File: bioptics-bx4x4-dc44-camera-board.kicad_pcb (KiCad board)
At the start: 4 copper layers, 260 x 187 mm, 475 parts, among them J1 RadEye1, J10 RadEye1, J11 RadEye1, J12 TagConnect_TC2030_SWD, J13 RadEye1, J14 RadEye1, J2 RadEye1, J3 USB_C_Receptacle_USB2.0, J4 TagConnect_TC2030_SWD, J5 TagConnect_TC2030_SWD, J6 TagConnect_TC2030_SWD, J7 RadEye1, J8 RadEye1, J9 TagConnect_TC2030_SWD, U1 AMS1117-3.3, U10 SRV05-4, U11 IS4xS32160F-xTL, U12 USB3300-EZK, U13 AMS1117-3.3, U14 STM32H753IITx, U15 CJ431, U16 7408, U17 CJ431, U18 AMS1117-3.3, U19 STM32H753IITx, U2 STM32H753IITx, U20 7408, U21 SN74AVC8T245PW, U22 AD5112, U23 INA849, U24 SN74AVC8T245PW, U25 AD5112, U26 INA849, U28 AMS1117-3.3, U29 STM32H753IITx, U3 SN74AVC8T245PW, U30 7408, U31 SN74AVC8T245PW, U32 AD5112, U33 INA849, U34 SN74AVC8T245PW, U35 AD5112, U36 INA849, U38 AMS1117-3.3, U39 STM32H753IITx, U4 AD5112, U40 7408, U41 SN74AVC8T245PW, U42 AD5112, U43 INA849, U44 SN74AVC8T245PW, U45 AD5112, U46 INA849, U5 INA849, U6 SN74AVC8T245PW, U7 AD5112, U8 INA849, U9 FP6291, Y1 24MHz

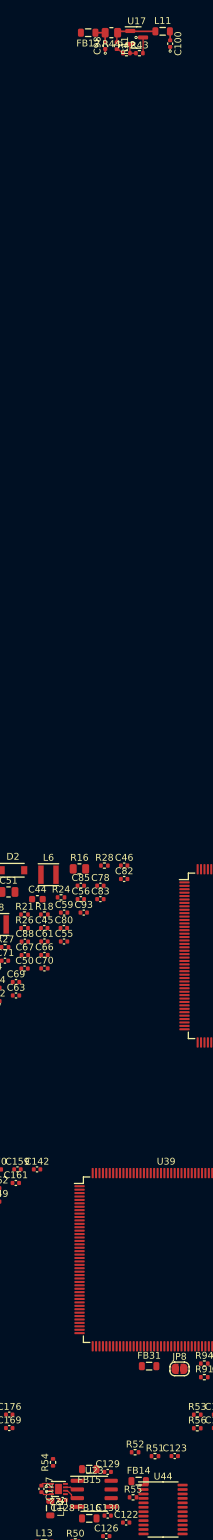
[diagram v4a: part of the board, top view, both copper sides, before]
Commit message: Delete PoC layouts on unplaced parts
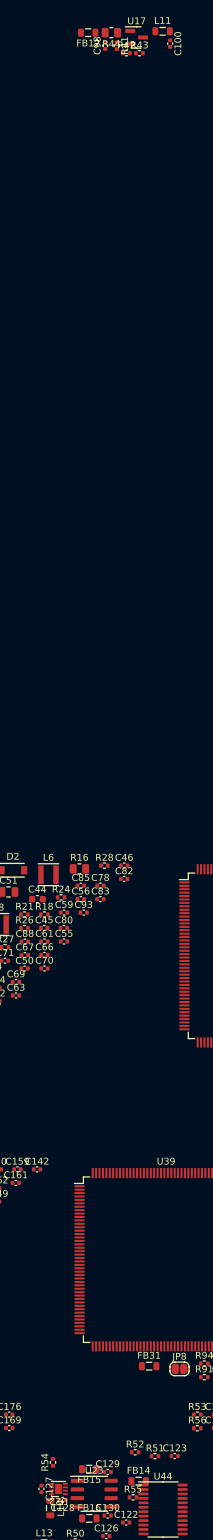
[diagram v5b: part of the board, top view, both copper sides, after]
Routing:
- net Net-(L11-Pad1): track 7.01 -> 0.00 mm
- net GND: track 209.4 -> 203.1 mm, vias 58 -> 55
- net Net-(U22-Pad2): track 3.59 -> 0.00 mm
- net Net-(C98-Pad2): track 2.89 -> 0.00 mm
- net Net-(R42-Pad2): track 2.19 -> 0.00 mm
- net /Sensor board 2/3v3: track 1.64 -> 0.00 mm
- net /3v8_2: track 1.32 -> 0.00 mm
- net Net-(R41-Pad2): track 0.94 -> 0.00 mm
- net /Sensor board 2/SCL_{1}: track 0.83 -> 0.00 mm, vias 1 -> 0
- net /Sensor board 2/SDA_{1}: track 0.78 -> 0.00 mm, vias 1 -> 0
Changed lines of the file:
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@@
   (segment (start 65.124168 32.58) (end 64.904168 32.8) (width 0.127) (layer "F.Cu") (net 4))
   (segment (start 120.4 65.288957) (end 120.4 65.258957) (width 0.127) (layer "F.Cu") (net 4))
-  (segment (start 440.0775 -55.44) (end 440.0775 -53.1775) (width 0.127) (layer "F.Cu") (net 4))
   (segment (start 48.6625 70.5) (end 48.6625 68.2375) (width 0.127) (layer "F.Cu") (net 4))
   (segment (start 120.4 65.258957) (end 121.55 64.108958) (width 0.127) (layer "F.Cu") (net 4))
@@
   (segment (start 34.983078 34.717499) (end 33.532501 34.717499) (width 0.127) (layer "F.Cu") (net 4))
   (segment (start 61.870062 52.935) (end 61.870062 55.785) (width 0.127) (layer "F.Cu") (net 4))
-  (segment (start 425.2 156.5) (end 425.2 156.4) (width 0.127) (layer "F.Cu") (net 4))
   (segment (start 106.2 36.058958) (end 106.199999 34.308957) (width 0.127) (layer "F.Cu") (net 4))
   (segment (start 53.3125 59.7) (end 53.3375 59.675) (width 0.127) (layer "F.Cu") (net 4))
@@
   (segment (start 49.475 47.100001) (end 50.5125 47.100001) (width 0.127) (layer "F.Cu") (net 4))
   (segment (start 114.28 35.288957) (end 114.25 35.258956) (width 0.127) (layer "F.Cu") (net 4))
-  (segment (start 425.2 156.4) (end 425.4 156.2) (width 0.127) (layer "F.Cu") (net 4))
   (segment (start 33.516922 56.233272) (end 34.996922 56.233272) (width 0.127) (layer "F.Cu") (net 4))
   (segment (start 98.67 56.858958) (end 98.1 56.858958) (width 0.127) (layer "F.Cu") (net 4))
@@
   (segment (start 35.67 49.935) (end 35.67 51.37) (width 0.127) (layer "F.Cu") (net 4))
   (segment (start 108.03 33.913957) (end 108 33.883957) (width 0.127) (layer "F.Cu") (net 4))
-  (segment (start 434.540001 -53.76) (end 434.54 -53.14) (width 0.254) (layer "F.Cu") (net 4))
   (segment (start 54.199999 68.82) (end 54.2 68.2) (width 0.254) (layer "F.Cu") (net 4))
   (segment (start 61.270062 50.62) (end 61.270062 49.335) (width 0.127) (layer "F.Cu") (net 4))
   (segment (start 137.075 48.93) (end 138.73 48.93) (width 0.127) (layer "F.Cu") (net 4))
-  (segment (start 440.0775 -53.1775) (end 440.04 -53.14) (width 0.127) (layer "F.Cu") (net 4))
   (segment (start 48.6625 68.2375) (end 48.7 68.2) (width 0.127) (layer "F.Cu") (net 4))
   (segment (start 126.475 44.408957) (end 127.949999 44.408957) (width 0.127) (layer "F.Cu") (net 4))
@@
   (segment (start 128 40.228957) (end 128.67 40.228956) (width 0.127) (layer "F.Cu") (net 4))
   (segment (start 120.4 65.288957) (end 120.4 65.958957) (width 0.127) (layer "F.Cu") (net 4))
-  (segment (start 425.4 156.2) (end 426.7 156.2) (width 0.127) (layer "F.Cu") (net 4))
   (segment (start 50.5125 47.100001) (end 50.5375 47.075001) (width 0.127) (layer "F.Cu") (net 4))
   (segment (start 35.67 51.37) (end 35.7 51.4) (width 0.127) (layer "F.Cu") (net 4))
@@
   (segment (start 137.075 47.66) (end 137.135 47.6) (width 0.127) (layer "F.Cu") (net 4))
   (segment (start 48.6625 70.5) (end 49.7 70.5) (width 0.254) (layer "F.Cu") (net 4))
-  (segment (start 440.0775 -55.44) (end 439.04 -55.44) (width 0.254) (layer "F.Cu") (net 4))
   (segment (start 55.2 47.750001) (end 54.1625 47.750001) (width 0.127) (layer "F.Cu") (net 4))
   (segment (start 67.837499 36.45) (end 67.0375 36.45) (width 0.127) (layer "F.Cu") (net 4))
@@
   (segment (start 132.125 54.01) (end 132.125 54.775) (width 0.127) (layer "F.Cu") (net 4))
   (segment (start 61.270062 50.835) (end 61.270062 50.585) (width 0.127) (layer "F.Cu") (net 4))
-  (segment (start 444.04 -54.06) (end 444.04 -53.44) (width 0.254) (layer "F.Cu") (net 4))
   (segment (start 44.7 69.12) (end 44.7 68.5) (width 0.254) (layer "F.Cu") (net 4))
   (segment (start 61.270062 49.335) (end 60.920062 48.985) (width 0.127) (layer "F.Cu") (net 4))
@@
   (via (at 53.3375 59.675) (size 0.45) (drill 0.2) (layers "F.Cu" "B.Cu") (net 4))
   (via (at 98.1 57.838957) (size 0.45) (drill 0.2) (layers "F.Cu" "B.Cu") (net 4))
-  (via (at 444.04 -53.44) (size 0.45) (drill 0.2) (layers "F.Cu" "B.Cu") (net 4))
   (via (at 44.7 68.5) (size 0.45) (drill 0.2) (layers "F.Cu" "B.Cu") (net 4))
   (via (at 47.4375 65.575) (size 0.45) (drill 0.2) (layers "F.Cu" "B.Cu") (net 4))
@@
   (via (at 128.7 60.108957) (size 0.45) (drill 0.2) (layers "F.Cu" "B.Cu") (net 4))
   (via (at 56.5 47.150001) (size 0.45) (drill 0.2) (layers "F.Cu" "B.Cu") (net 4))
-  (via (at 439.04 -55.44) (size 0.45) (drill 0.2) (layers "F.Cu" "B.Cu") (net 4))
   (via (at 49.7 70.5) (size 0.45) (drill 0.2) (layers "F.Cu" "B.Cu") (net 4))
   (via (at 99.011043 46.738956) (size 0.45) (drill 0.2) (layers "F.Cu" "B.Cu") (net 4))
@@
   (via (at 45.083078 59.096728) (size 0.45) (drill 0.2) (layers "F.Cu" "B.Cu") (net 4))
   (via (at 54.2 68.2) (size 0.45) (drill 0.2) (layers "F.Cu" "B.Cu") (net 4))
-  (via (at 434.54 -53.14) (size 0.45) (drill 0.2) (layers "F.Cu" "B.Cu") (net 4))
   (via (at 50.5375 47.775001) (size 0.45) (drill 0.2) (layers "F.Cu" "B.Cu") (net 4))
   (via (at 35.7 51.4) (size 0.45) (drill 0.2) (layers "F.Cu" "B.Cu") (net 4))
@@
   (segment (start 138.82 46.4) (end 137.1 46.4) (width 0.127) (layer "F.Cu") (net 165))
   (segment (start 137.1 44.7625) (end 137.1 46.4) (width 0.127) (layer "F.Cu") (net 165))
-  (segment (start 434.5275 -56.14) (end 434.5275 -54.7525) (width 0.254) (layer "F.Cu") (net 167))
-  (segment (start 434.5275 -54.7525) (end 434.54 -54.74) (width 0.254) (layer "F.Cu") (net 167))
-  (segment (start 434.5275 -56.14) (end 433.04 -56.14) (width 0.254) (layer "F.Cu") (net 167))
-  (segment (start 425.2 157.46) (end 425.54 157.8) (width 0.127) (layer "F.Cu") (net 168))
-  (segment (start 425.54 157.8) (end 426.7 157.8) (width 0.127) (layer "F.Cu") (net 168))
-  (segment (start 444.04 -55.02) (end 444.04 -56.34) (width 0.254) (layer "F.Cu") (net 169))
   (segment (start 109.9 35.988958) (end 110.5 35.388958) (width 0.127) (layer "F.Cu") (net 190))
   (segment (start 34.4 49.935) (end 34.4 50.6) (width 0.127) (layer "F.Cu") (net 190))
@@
   (segment (start 52.4 71.4) (end 52.5 71.3) (width 0.254) (layer "F.Cu") (net 267))
   (segment (start 46.8625 71.4) (end 52.4 71.4) (width 0.254) (layer "F.Cu") (net 267))
-  (segment (start 436.24 -54.75) (end 436.24 -55.94) (width 0.127) (layer "F.Cu") (net 268))
-  (segment (start 436.24 -55.94) (end 436.34 -56.04) (width 0.127) (layer "F.Cu") (net 268))
-  (segment (start 436.34 -56.34) (end 436.24 -56.24) (width 0.254) (layer "F.Cu") (net 268))
-  (segment (start 441.8775 -56.34) (end 436.34 -56.34) (width 0.254) (layer "F.Cu") (net 268))
   (segment (start 44.160624 46.460624) (end 44.939376 46.460624) (width 0.127) (layer "F.Cu") (net 269))
   (segment (start 44.939376 46.460624) (end 45 46.4) (width 0.127) (layer "F.Cu") (net 269))
@@
   (segment (start 50.59 68.2) (end 50.59 69.49) (width 0.127) (layer "F.Cu") (net 293))
   (segment (start 49.71 68.2) (end 50.6 68.2) (width 0.127) (layer "F.Cu") (net 293))
-  (segment (start 437.13 -53.14) (end 437.04 -53.14) (width 0.127) (layer "F.Cu") (net 296))
-  (segment (start 437.04 -53.14) (end 436.44 -53.74) (width 0.127) (layer "F.Cu") (net 296))
-  (segment (start 438.15 -54.43) (end 438.14 -54.44) (width 0.127) (layer "F.Cu") (net 297))
-  (segment (start 438.15 -53.14) (end 438.15 -54.43) (width 0.127) (layer "F.Cu") (net 297))
-  (segment (start 439.03 -53.14) (end 438.14 -53.14) (width 0.127) (layer "F.Cu") (net 297))
-  (segment (start 426.685 156.75) (end 426 156.75) (width 0.127) (layer "F.Cu") (net 309))
-  (segment (start 426 156.75) (end 425.9 156.65) (width 0.127) (layer "F.Cu") (net 309))
-  (via (at 425.9 156.65) (size 0.45) (drill 0.2) (layers "F.Cu" "B.Cu") (net 309))
-  (segment (start 426.05 157.25) (end 425.95 157.35) (width 0.127) (layer "F.Cu") (net 310))
-  (segment (start 426.685 157.25) (end 426.05 157.25) (width 0.127) (layer "F.Cu") (net 310))
-  (via (at 425.95 157.35) (size 0.45) (drill 0.2) (layers "F.Cu" "B.Cu") (net 310))
   (segment (start 132.125 52.74) (end 133.34 52.74) (width 0.127) (layer "F.Cu") (net 368))
   (segment (start 133.34 52.74) (end 133.4 52.8) (width 0.127) (layer "F.Cu") (net 368))
@@
   (segment (start 58.935062 56.47) (end 60.770062 54.635) (width 0.127) (layer "F.Cu") (net 915))
   (segment (start 58.278394 56.47) (end 58.935062 56.47) (width 0.127) (layer "F.Cu") (net 915))
-  (segment (start 428.715 157.25) (end 429 157.25) (width 0.127) (layer "F.Cu") (net 920))
-  (segment (start 429.45 156.75) (end 429.75 157.05) (width 0.127) (layer "F.Cu") (net 920))
-  (segment (start 429.75 157.05) (end 430.5 157.05) (width 0.127) (layer "F.Cu") (net 920))
-  (segment (start 429.6 157.85) (end 429.6 158.4) (width 0.127) (layer "F.Cu") (net 920))
-  (segment (start 428.715 156.75) (end 429.45 156.75) (width 0.127) (layer "F.Cu") (net 920))
-  (segment (start 429 157.25) (end 429.6 157.85) (width 0.127) (layer "F.Cu") (net 920))
   (zone (net 0) (net_name "") (layer "F.Cu") (hatch edge 0.508)
     (connect_pads (clearance 0))

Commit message: Layout remaining sensors
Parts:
- C235: moved to F.Cu
- moved JP7 561.9 mm to (-73.6, -1.85), turned to 180 degrees
- moved JP8 541.5 mm to (-78.5, 2.60), turned to 180 degrees
- moved JP5 515.7 mm to (-73.6, -51.5), turned to 180 degrees
- moved JP6 498.7 mm to (-78.5, -47.0), turned to 180 degrees
- moved C134 479.3 mm to (33.5, 104.8), turned to -90 degrees
- moved FB17 467.9 mm to (33.5, 101.9), turned to 90 degrees
- moved R60 467.1 mm to (43.0, 114.4), turned to 45 degrees
- moved C136 463.2 mm to (33.5, 108.8), turned to -90 degrees
- moved L15 459.8 mm to (33.1, 111.6), turned to -90 degrees
- moved C133 459.7 mm to (46.9, 106.3)
- moved R59 458.5 mm to (42.3, 113.7), turned to 45 degrees
- moved R58 458.0 mm to (45.8, 100.1), turned to 180 degrees
- moved J6 452.1 mm to (34.4, 98.3)
- moved R49 451.5 mm to (33.1, 94.2), turned to -90 degrees
- moved C132 448.0 mm to (51.7, 106.3)
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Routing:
- net GND: track 203.1 -> 803.3 mm, vias 55 -> 214
- net Net-(J6-Pad2): track 0.00 -> 106.3 mm, vias 0 -> 4
- net Net-(J9-Pad2): track 0.00 -> 106.3 mm, vias 0 -> 4
- net Net-(J12-Pad2): track 0.00 -> 106.3 mm, vias 0 -> 4
- net /Sensor board 4/LINE_{2}: track 0.00 -> 104.5 mm, vias 0 -> 4
- net /Sensor board 3/LINE_{2}: track 0.00 -> 104.5 mm, vias 0 -> 4
- net /Sensor board 2/LINE_{2}: track 0.00 -> 104.5 mm, vias 0 -> 4
- net /Sensor board 4/Sensor 2/TRIG_OUT_{5V}: track 0.00 -> 99.4 mm, vias 0 -> 4
- net /Sensor board 3/Sensor 2/TRIG_OUT_{5V}: track 0.00 -> 99.4 mm, vias 0 -> 4
- net /Sensor board 2/Sensor 2/TRIG_OUT_{5V}: track 0.00 -> 99.4 mm, vias 0 -> 4
- net /Sensor board 4/MCUL_~{RST}: track 0.00 -> 99.2 mm, vias 0 -> 4
- net /Sensor board 3/MCUL_~{RST}: track 0.00 -> 99.2 mm, vias 0 -> 4
- net /Sensor board 2/MCUL_~{RST}: track 0.00 -> 99.2 mm, vias 0 -> 4
- net /Sensor board 2/LINE_{1}: track 0.00 -> 98.7 mm, vias 0 -> 5
- net /Sensor board 3/LINE_{1}: track 0.00 -> 98.7 mm, vias 0 -> 5
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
